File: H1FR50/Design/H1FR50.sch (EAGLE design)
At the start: 49 parts, among them J1 MOLEX_INC_0732511150MOLEX_INC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, P1 HEXABIT_17.32_X2_NO_P5, U1 STM32F091RBT6STMICROELECTRONI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, U2 TPS22943DCKR, U3 BGA824N6, U4 TESEO-LIV3F, U5 B39162B4327P810, X1 XTALL_CSTCE8M00G52

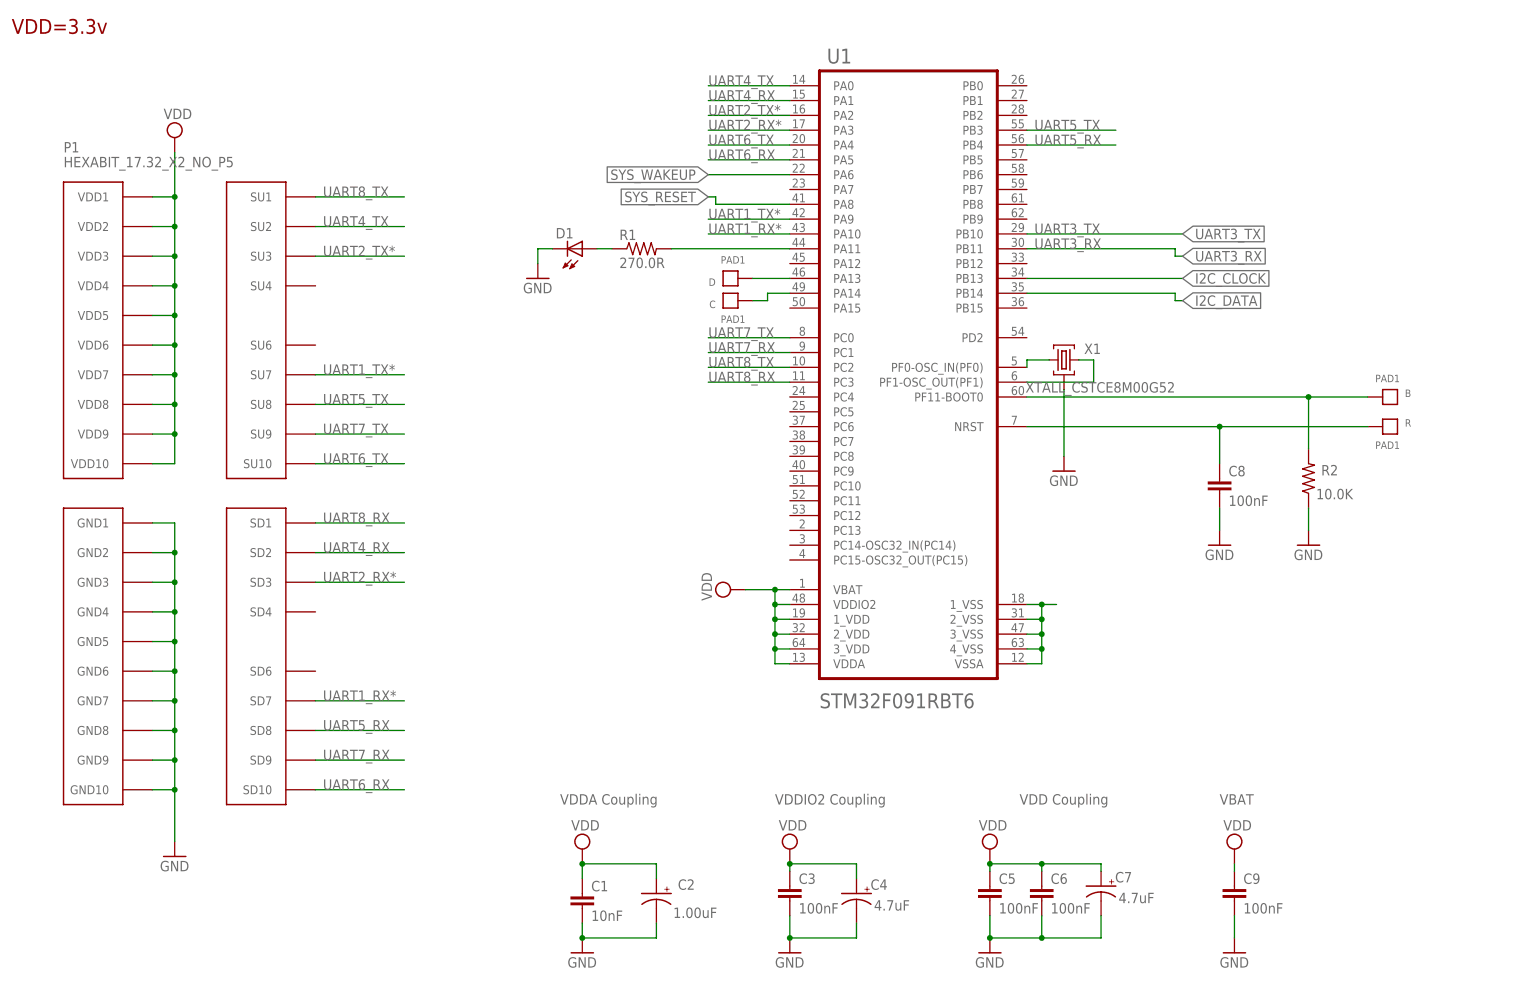
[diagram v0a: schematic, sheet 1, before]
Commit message: -Changing the MC to STM32G0B1CEU6N -Changing the GPS Module to SAM-M8Q-0-10 u-blox
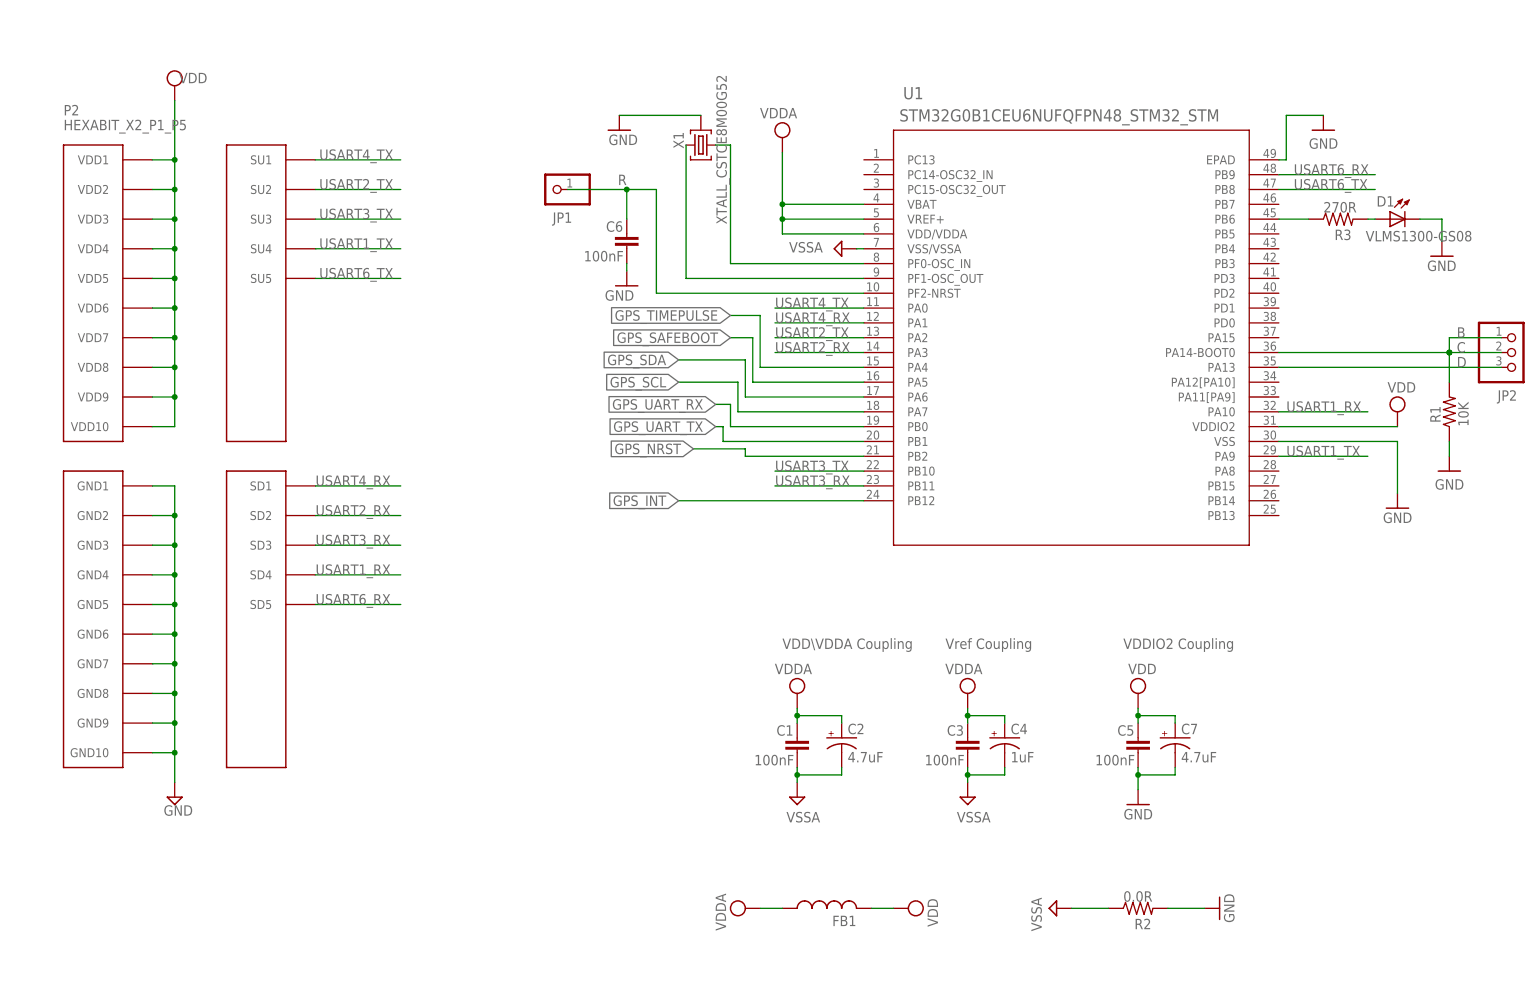
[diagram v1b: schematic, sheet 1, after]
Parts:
- removed B, C, D, R: PAD1, Hexabitz:PAD1
- removed C14: 3.9pF, HEXABITZ_RCLS:C-0402
- removed C15: 120pF, HEXABITZ_RCLS:C-0402
- removed C16: 1nF, HEXABITZ_RCLS:C-0402
- removed C17: 1.00uF, HEXABITZ_RCLS:C-0402
- removed C18: 2.2uF, HEXABITZ_RCLS:C-0402
- removed C19: 56pF, HEXABITZ_RCLS:C-0201C0201
- removed D2: ESDARF02-1BU2CK, HEXABITZ_RCLS:ESDARF02-1BU2CK
- removed FB4: 27nH, HEXABITZ_RCLS:FB-0402
- removed J1: MOLEX_INC_0732511150MOLEX_INC_0732511150_0_0, HEXABITZ_CONNECTION_PARTS:MOLEX_INC_0732511150MOLEX_INC_0732511150_0_0
- removed P1: HEXABIT_17.32_X2_NO_P5, hexabitz_connectors:HEXABIT_17.32_X2_NO_P5
- removed R10, R12: 0.0R, HEXABITZ_RCLS:R-0402
- removed R11, R13: DNP, HEXABITZ_RCLS:R-0402
- removed R14: 100k, HEXABITZ_RCLS:R-0603
- removed U3: BGA824N6, HEXABITZ_ICs:BGA824N6
- removed U4: TESEO-LIV3F, HEXABITZ_ICs:TESEO-LIV3F
- removed U5: B39162B4327P810, HEXABITZ_ICs:B39162B4327P810
- added FB1: (no value), HEXABITZ_RCLS:FB-0603
- added JP1: R, HEXABITZ_USER_INTERFACE_PARTS:PINHD-1X1
- added JP2: (no value), pinhead:PINHD-1X3
- added P2: HEXABIT_X2_P1_P5, hexabitz_connectors:HEXABIT_X2_P1_P5
- added Q1, Q2: MMBT3904LT1, HEXABITZ_RCLS:MMBT3904LT1
- added R3: 270R, HEXABITZ_RCLS:R-0603
- C1: value 10nF -> 100nF; device Hexabitz:C-0603 -> HEXABITZ_RCLS:C-0603; CAPACITANCE 10nF -> (none); MFN KEMET -> (none); MPN C0603C103K5RACTU -> (none); OCTOPART_URL https://octopart.com/c0603c103k5ractu-kemet-133094?r=sp&s=R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 -> (none); TOLERANCE 10% -> (none); VOLTAGE_RATING 50V -> (none)
- C10: value 56pF -> 100nF; device HEXABITZ_RCLS:C-0201C0201 -> HEXABITZ_RCLS:C-0603; MFN Murata -> (none); MPN GRM0335C1E560GA01D -> (none); OCTOPART_URL https://octopart.com/grm0335c1e560ga01d-murata-24611383?r=sp -> (none)
- C11: value 10nF -> 4.7uF; device HEXABITZ_RCLS:C-0402 -> HEXABITZ_RCLS:C-0805-POL; CAPACITANCE 10nF -> (none); MFN TDK -> (none); MPN CGA2B3X7R1H103K050BE -> (none); OCTOPART_URL https://octopart.com/cga2b3x7r1h103k050be-tdk-68305469?r=sp -> (none)
- C12: value 56pF -> 100nF; device HEXABITZ_RCLS:C-0402 -> HEXABITZ_RCLS:C-0603; CAPACITANCE 56pF -> (none); MFN Murata -> (none); MPN GRM1555C1H560JA01D -> (none); OCTOPART_URL https://octopart.com/grm1555c1h560ja01d-murata-15197568?r=sp -> (none)
- C13: value 120pF -> 4.7uF; device HEXABITZ_RCLS:C-0402 -> HEXABITZ_RCLS:C-0805-POL; CAPACITANCE 120pF -> (none); MFN Murata -> (none); MPN GRM1555C1H121JA01D -> (none); OCTOPART_URL https://octopart.com/grm1555c1h121ja01d-murata-196010?r=sp -> (none)
- C2: value 1.00uF -> 4.7uF; device Hexabitz:C-0805-POL -> HEXABITZ_RCLS:C-0805-POL; CAPACITANCE 1.00uF -> (none); MFN Yageo -> (none); MPN CC0805KKX7R7BB105 -> (none); OCTOPART_URL https://octopart.com/cc0805kkx7r7bb105-yageo-8376555?r=sp&s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 -> (none); TOLERANCE 10% -> (none); VOLTAGE_RATING 16V -> (none)
- C3, C6, C8: device Hexabitz:C-0603 -> HEXABITZ_RCLS:C-0603; CAPACITANCE 100nF -> (none); MFN KEMET -> (none); MPN C0603C104K8RACTU -> (none); OCTOPART_URL https://octopart.com/c0603c104k8ractu-kemet-145075?r=sp&s=9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 -> (none); TOLERANCE 10% -> (none); VOLTAGE_RATING 10V -> (none)
- C4: value 4.7uF -> 1uF; device Hexabitz:C-0805-POL -> HEXABITZ_RCLS:C-0805-POL; CAPACITANCE 4.7uF -> (none); MFN Murata -> (none); MPN GRM21BC81E475KA12L -> (none); OCTOPART_URL https://octopart.com/grm21bc81e475ka12l-murata-10331911?r=s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 -> (none); TOLERANCE 10% -> (none); VOLTAGE_RATING 25V -> (none)
- C5: device Hexabitz:C-0603 -> HEXABITZ_RCLS:C-0603; CAPACITANCE 100nF -> (none); MFN KEMET -> (none); MPN C0603C104K8RACTU -> (none); OCTOPART_URL https://octopart.com/c0603c104k8ractu-kemet-145075?r=sp&s=9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 -> (none); TOLERANCE 10% -> (none); VOLTAGE_RATING 10 -> (none)
- C7: device Hexabitz:C-0805-POL -> HEXABITZ_RCLS:C-0805-POL; CAPACITANCE 4.7uF -> (none); MFN Murata -> (none); MPN GRM21BC81E475KA12L -> (none); OCTOPART_URL https://octopart.com/grm21bc81e475ka12l-murata-10331911?r=s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 -> (none); TOLERANCE 10% -> (none); VOLTAGE_RATING 25V -> (none)
- C9: value 100nF -> 4.7uF; device Hexabitz:C-0603 -> HEXABITZ_RCLS:C-0805-POL; CAPACITANCE 100nF -> (none); MFN KEMET -> (none); MPN C0603C104K8RACTU -> (none); OCTOPART_URL https://octopart.com/c0603c104k8ractu-kemet-145075?r=sp&s=9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 -> (none); TOLERANCE 10V -> (none); VOLTAGE_RATING 10% -> (none)
- FB2: value 56nH -> BLM18KG601SN1D; device HEXABITZ_RCLS:FB-0402 -> HEXABITZ_RCLS:FB-0603; MFN Murata -> (none); MPN LQW15AN6N8G00D -> (none); OCTOPART_URL https://octopart.com/lqw15an6n8g00d-murata-7896134?r=sp -> (none)
- FB3: value 6.8nH -> BLM18KG601SN1D; device HEXABITZ_RCLS:FB-0402 -> HEXABITZ_RCLS:FB-0603; MFN Würth Elektronik -> (none); MPN 744784156A -> (none); OCTOPART_URL https://octopart.com/744784156a-w%C3%BCrth+elektronik-46756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 -> (none)
- R1: value 270.0R -> 10K; device Hexabitz:R-0603 -> HEXABITZ_RCLS:R-0603; MFN Yageo -> (none); MPN RC0603FR-07270RL -> (none); OCTOPART_URL https://octopart.com/search?q=RC0603FR-07270RL&start=0 -> (none); RESISTANCE 270.0 Ohm -> (none); TOLERANCE 1% -> (none)
- R2: value 10.0K -> 0.0R; device Hexabitz:R-0603 -> HEXABITZ_RCLS:R-0603; MFN Yageo -> (none); MPN RC0603JR-0710KL -> (none); OCTOPART_URL https://octopart.com/search?q=RC0603JR-0710KL&start=0 -> (none); RESISTANCE 10.0K Ohm -> (none); TOLERANCE 5% -> (none)
- R4: value 0.0R -> 10K; device HEXABITZ_RCLS:R-0402 -> HEXABITZ_RCLS:R-0603
- R5: value 10.0k -> 10K; device HEXABITZ_RCLS:R-0402 -> HEXABITZ_RCLS:R-0603; MFN TE Connectivity -> (none); MPN CRGCQ0402F10K -> (none); OCTOPART_URL https://octopart.com/crgcq0402f10k-te+connectivity-91017932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 -> (none); RESISTANCE 10.0K -> (none); TOLERANCE ±1% -> (none)
- R6, R7: value DNP -> 10K; device HEXABITZ_RCLS:R-0402 -> HEXABITZ_RCLS:R-0603
- R8: value 0.0R -> 150R; device HEXABITZ_RCLS:R-0402 -> HEXABITZ_RCLS:R-0603; MPN (none) -> CRCW0603150RFKEA
- R9: value DNP -> 150R; device HEXABITZ_RCLS:R-0402 -> HEXABITZ_RCLS:R-0603; MPN (none) -> CRCW0603150RFKEA
- U1: value STM32F091RBT6STMICROELECTRONICS_STM32F091RBT6_0_1 -> STM32G0B1CEU6NUFQFPN48_STM32_STM; device Hexabitz:STM32F091RBT6STMICROELECTRONICS_STM32F091RBT6_0_1 -> HEXABITZ_ICs:STM32G0B1CEU6NUFQFPN48_STM32_STM; MFN STMicroelectronics -> (none); OCTOPART_URL https://octopart.com/stm32f091rbt6-stmicroelectronics-51988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 -> (none)
- U2: value TPS22943DCKR -> SAM-M8Q-0-10; device HEXABITZ_ICs:TPS22943DCKR -> SAM-M8Q-0-10:SAM-M8Q-0-10
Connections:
- removed net ANTOFF: R10.2, R4.2, R5.1, U4.ANT_OFF
- removed net ANT_IN: R13.1, R6.1
- removed net B1: B.P$1, R2.2, U1.PF11-BOOT0
- removed net I2C_CLOCK: U1.PB13, U4.SCL
- removed net I2C_DATA: U1.PB14, U4.SDA
- removed net N$13: U3.AO, U5.INPUT
- removed net N$16: R4.1, R7.1, U3.PON
- removed net N$17: C15.1, U5.OUTPUT
- removed net N$19: C16.1, R8.1, U3.VCC
- removed net N$20: C17.1, R9.1, U2.VOUT
- removed net N$22: R10.1, R11.2, U2.ON
- removed net N$23: C18.1, R11.1, R12.2, R14.1, U2.VIN
- removed net R1: C8.1, R.P$1, U1.NRST
- removed net RF_IN: C15.2, R6.2, U4.RF_IN
- removed net SYS_RESET: U1.PA8, U4.SYS_RSTN
- removed net SYS_WAKEUP: U1.PA6, U4.WAKE-UP
- removed net UART1_RX*: P1.SD7, U1.PA10
- removed net UART1_TX*: P1.SU7, U1.PA9
- removed net UART2_RX*: P1.SD3, U1.PA3
- removed net UART2_TX*: P1.SU3, U1.PA2
- removed net UART3_RX: U1.PB11, U4.RX
- removed net UART3_TX: U1.PB10, U4.TX
- removed net UART4_RX: P1.SD2, U1.PA1
- removed net UART4_TX: P1.SU2, U1.PA0
- removed net UART5_RX: P1.SD8, U1.PB4
- removed net UART5_TX: P1.SU8, U1.PB3
- removed net UART6_RX: P1.SD10, U1.PA5
- removed net UART6_TX: P1.SU10, U1.PA4
- removed net UART7_RX: P1.SD9, U1.PC1
- removed net UART7_TX: P1.SU9, U1.PC0
- removed net UART8_RX: P1.SD1, U1.PC3
- removed net UART8_TX: P1.SU1, U1.PC2
- removed net VCC_RF: C19.2, R12.1, R7.2, R8.2, U4.VCC_RF
- removed net VCC_RF1: C10.2, FB4.1, U4.VBATT, U4.VCC, U4.VCC_IO
- new net C: JP2.1, JP2.2, R1.2, U1.PA14-BOOT0
- new net D: JP2.3, U1.PA13
- new net GPS_INT: U1.PB12, U2.EXTINT0
- new net GPS_NRST: R4.2, U1.PB2
- new net GPS_SAFEBOOT: R5.2, U1.PA5
- new net GPS_SCL: R8.2, U1.PA7
- new net GPS_SDA: R9.2, U1.PA6
- new net GPS_TIMEPULSE: U1.PA4, U2.TIMEPULSE
- new net GPS_UART_RX: FB2.2, U1.PB0
- new net GPS_UART_TX: FB3.2, U1.PB1
- new net N$14: R3.1, U1.PB6
- new net N$8: Q1.B, R5.1
- new net USART1_RX: P2.SD4, U1.PA10
- new net USART1_TX: P2.SU4, U1.PA9
- new net USART2_RX: P2.SD2, U1.PA3
- new net USART2_TX: P2.SU2, U1.PA2
- new net USART3_RX: P2.SD3, U1.PB11
- new net USART3_TX: P2.SU3, U1.PB10
- new net USART4_RX: P2.SD1, U1.PA1
- new net USART4_TX: P2.SU1, U1.PA0
- new net USART6_RX: P2.SD5, U1.PB9
- new net USART6_TX: P2.SU5, U1.PB8
- new net VDDA: C1.1, C2.+, C3.1, C4.+, FB1.1, U1.VBAT, U1.VDD/VDDA, U1.VREF+
- new net VSSA: C1.2, C2.-, C3.2, C4.-, R2.1, U1.VSS/VSSA
- net GND: now also C10.2, C11.-, C12.2, C13.-, C9.-, P2.GND1, P2.GND10, P2.GND2, P2.GND3, P2.GND4, P2.GND5, P2.GND6, P2.GND7, P2.GND8, P2.GND9, Q1.E, Q2.E, R1.1, R2.2, U1.EPAD, U1.VSS; no longer C1.2, C10.1, C11.1, C12.1, C14.1, C16.2, C17.2, C18.2, C19.1, C2.-, C3.2, C4.-, C9.2, D2.1, J1.MNT_1, J1.MNT_2, J1.MNT_3, J1.MNT_4, P1.GND1, P1.GND10, P1.GND2, P1.GND3, P1.GND4, P1.GND5, P1.GND6, P1.GND7, P1.GND8, P1.GND9, R2.1, R5.2, U1.1_VSS, U1.2_VSS, U1.3_VSS, U1.4_VSS, U1.VSSA, U3.GND, U3.GND-RF, U4.GND, U4.GND_RF_1, U4.GND_RF_2, U5.GND
- net N$1: now also D1.A, R3.2; no longer C13.2, C14.2, FB3.1
- net N$10: now also FB3.1, U2.TXD; no longer R1.2, U1.PA11
- net N$11: now also R8.1, U2.SCL; no longer C12.2, FB2.1, R9.2
- net N$12: now also R9.1, U2.SDA; no longer FB3.2, U3.AI
- net N$2: now also U1.PF0-OSC_IN, X1.3; no longer R14.2, U2.OC
- net N$3: now also U1.PF1-OSC_OUT, X1.1; no longer C13.1, D2.2, FB2.2, J1.1, R13.2
- net N$4: now also Q2.C, R7.1, U2.!RESET; no longer D1.A, R1.1
- net N$5: now also C6.1, JP1.1, U1.PF2-NRST; no longer U1.PF0-OSC_IN(PF0), X1.1
- net N$6: now also Q1.C, R6.1, U2.!SAFEBOOT; no longer U1.PF1-OSC_OUT(PF1), X1.3
- net N$7: now also Q2.B, R4.1; no longer D.P$1, U1.PA13
- net N$9: now also FB2.1, U2.RXD; no longer C.P$1, U1.PA14
- net VDD: now also C10.1, C11.+, C12.1, C13.+, C8.1, C9.+, FB1.2, P2.VDD1, P2.VDD10, P2.VDD2, P2.VDD3, P2.VDD4, P2.VDD5, P2.VDD6, P2.VDD7, P2.VDD8, P2.VDD9, R6.2, R7.2, U2.VCC, U2.VCC_IO, U2.V_BCKP; no longer C1.1, C11.2, C2.+, C3.1, C4.+, C6.1, C9.1, FB4.2, P1.VDD1, P1.VDD10, P1.VDD2, P1.VDD3, P1.VDD4, P1.VDD5, P1.VDD6, P1.VDD7, P1.VDD8, P1.VDD9, U1.1_VDD, U1.2_VDD, U1.3_VDD, U1.VBAT, U1.VDDA
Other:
- note added: "B"
- note added: "GPS Module"
- note added: "I2C2"
- note added: "Ibrahim Zaeiter"
- note added: "USART5"
- note added: "VDD=3.3 Volts"
- note added: "VDD\VDDA Coupling"
- note added: "Vref Coupling"
- note removed: "Anas Kaadan"
- note removed: "TESEO-LIV3F GNSS Module"
- note removed: "VBAT"
- note removed: "VDD Coupling"
- note removed: "VDD=3.3v"
- note removed: "VDDA Coupling"
- moved on the sheet: C1, C10, C12, C2, C3, C4, C5, C6, C7, D1, R1, R2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

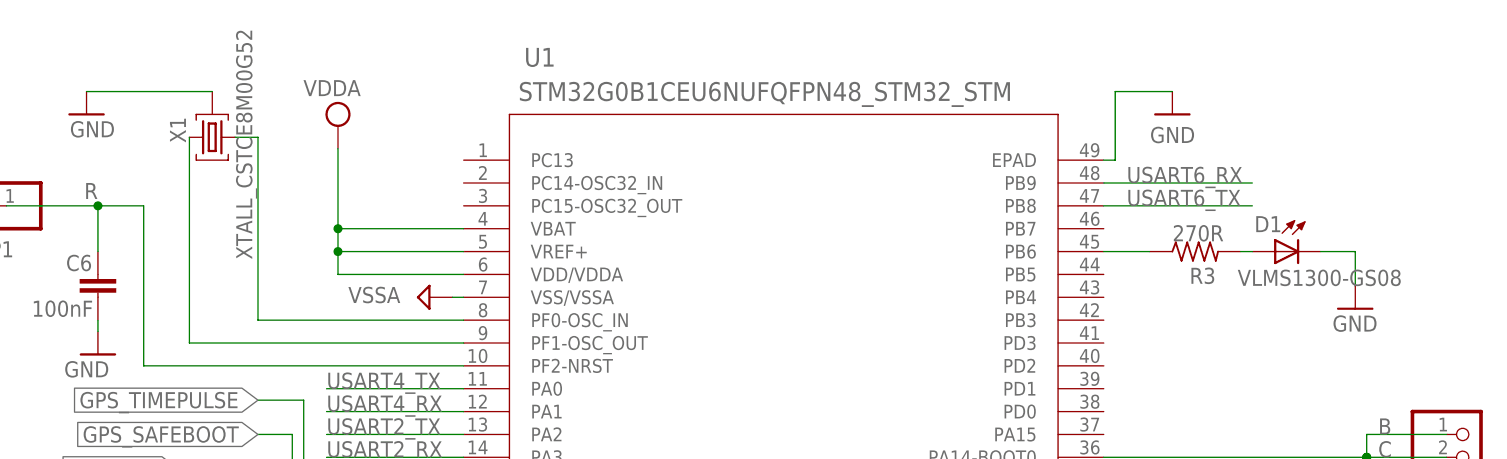
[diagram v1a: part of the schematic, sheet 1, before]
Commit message: -Correcting some documentaion issues
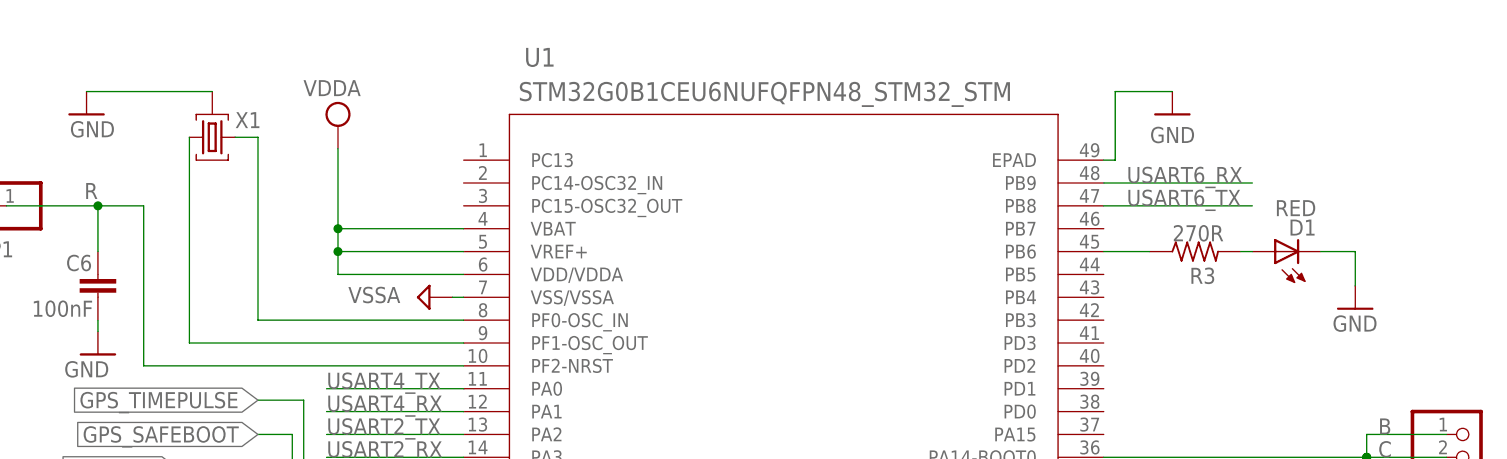
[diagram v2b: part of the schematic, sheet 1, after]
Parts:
- D1: value VLMS1300-GS08 -> RED; device Hexabitz:VLMS1300-GS08 -> HEXABITZ_USER_INTERFACE_PARTS:VLMS1300-GS08; MFN Vishay -> (none); MPN VLMS1300-GS08 -> (none); OCTOPART_URL https://octopart.com/vlms1300-gs08-vishay-21709201?r=sp&s=_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 -> (none)
- X1: value XTALL_CSTCE8M00G52 -> (none); device Hexabitz:XTALL_CSTCE8M00G52 -> HEXABITZ_RCLS:XTALL_CSTCE8M00G52
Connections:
- net N$2: now also X1.1; no longer X1.3
- net N$3: now also X1.3; no longer X1.1
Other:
- moved on the sheet: D1
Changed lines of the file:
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@@
 <?xml version="1.0" encoding="utf-8"?>
 <!DOCTYPE eagle SYSTEM "eagle.dtd">
-<eagle version="9.6.2">
+<eagle version="9.6.1">
 <drawing>
 <settings>
@@
 </classes>
 <parts>
-<part name="D1" library="Hexabitz" deviceset="VLMS1300-GS08" device="" value="VLMS1300-GS08">
-<attribute name="MFN" value="Vishay"/>
-<attribute name="MPN" value="VLMS1300-GS08"/>
-<attribute name="OCTOPART_URL" value="https://octopart.com/vlms1300-gs08-vishay-21709201?r=sp&amp;s=_gcP4_q8T1SC6PJQPTQ9yA"/>
-</part>
-<part name="X1" library="Hexabitz" deviceset="XTALL_CSTCE8M00G52" device="" value="XTALL_CSTCE8M00G52"/>
 <part name="GND1" library="supply1" library_urn="urn:adsk.eagle:library:371" deviceset="GND" device=""/>
 <part name="SUPPLY1" library="supply2" library_urn="urn:adsk.eagle:library:372" deviceset="VDD" device=""/>
 <part name="SUPPLY2" library="supply2" library_urn="urn:adsk.eagle:library:372" deviceset="GND" device=""/>
-<part name="P2" library="hexabitz_connectors" library_urn="urn:adsk.eagle:library:20064578" deviceset="HEXABIT_X2_P1_P5" device="" package3d_urn="urn:adsk.eagle:package:28065030/1"/>
+<part name="P2" library="hexabitz_connectors" library_urn="urn:adsk.eagle:library:20064578" deviceset="HEXABIT_X2_P1_P5" device="" package3d_urn="urn:adsk.eagle:package:28065030/1" override_package3d_urn="urn:adsk.eagle:package:28065030/2" override_package_urn="urn:adsk.eagle:footprint:28065029/1"/>
 <part name="SUPPLY14" library="supply2" deviceset="VDD" device=""/>
 <part name="SUPPLY15" library="supply2" deviceset="VCC" device="" value="VDDA"/>
@@
 <part name="SUPPLY9" library="supply2" deviceset="VDD" device=""/>
 <part name="JP2" library="pinhead" deviceset="PINHD-1X3" device="" package3d_urn="urn:adsk.eagle:package:22458/2"/>
-<part name="U2" library="SAM-M8Q-0-10" deviceset="SAM-M8Q-0-10" device=""/>
+<part name="U2" library="SAM-M8Q-0-10" deviceset="SAM-M8Q-0-10" device="" override_package3d_urn="urn:adsk.eagle:package:37789442/2" override_package_urn="urn:adsk.eagle:footprint:37789443/1"/>
 <part name="SUPPLY5" library="supply2" deviceset="VDD" device=""/>
 <part name="GND4" library="supply1" library_urn="urn:adsk.eagle:library:371" deviceset="GND" device=""/>
@@
 <attribute name="MPN" value="CRCW0603150RFKEA"/>
 </part>
-<part name="U1" library="HEXABITZ_ICs" library_urn="urn:adsk.eagle:library:20064554" deviceset="STM32G0B1CEU6N" device="UFQFPN48_STM32_STM" package3d_urn="urn:adsk.eagle:package:33906703/3"/>
+<part name="U1" library="HEXABITZ_ICs" library_urn="urn:adsk.eagle:library:20064554" deviceset="STM32G0B1CEU6N" device="UFQFPN48_STM32_STM" package3d_urn="urn:adsk.eagle:package:33906703/4"/>
+<part name="D1" library="HEXABITZ_USER_INTERFACE_PARTS" library_urn="urn:adsk.eagle:library:20064563" deviceset="VLMS1300-GS08" device="" package3d_urn="urn:adsk.eagle:package:20064571/2" value="RED"/>
+<part name="X1" library="HEXABITZ_RCLS" library_urn="urn:adsk.eagle:library:20064561" deviceset="XTALL_CSTCE8M00G52" device="" package3d_urn="urn:adsk.eagle:package:20410717/1" override_package3d_urn="urn:adsk.eagle:package:20410717/2" override_package_urn="urn:adsk.eagle:footprint:20410716/1"/>
 </parts>
 <sheets>
@@
 </plain>
 <instances>
-<instance part="D1" gate="G$1" x="251.46" y="168.91" smashed="yes" rot="MR0">
-<attribute name="NAME" x="252.222" y="171.069" size="1.778" layer="95" rot="MR0"/>
-<attribute name="VALUE" x="265.557" y="165.1" size="1.778" layer="96" rot="MR0"/>
-</instance>
-<instance part="X1" gate="G$1" x="133.35" y="181.61" smashed="yes" rot="MR180">
-<attribute name="NAME" x="128.651" y="180.975" size="1.778" layer="95" rot="MR90"/>
-<attribute name="VALUE" x="137.795" y="193.675" size="1.778" layer="96" rot="MR270"/>
-</instance>
 <instance part="GND1" gate="1" x="260.35" y="162.56" smashed="yes">
 <attribute name="VALUE" x="257.81" y="160.02" size="1.778" layer="96"/>
@@
 <attribute name="VALUE" x="167.3552" y="185.6486" size="2.083" layer="96" ratio="6"/>
 </instance>
+<instance part="D1" gate="G$1" x="251.46" y="168.91" smashed="yes" rot="R180">
+<attribute name="NAME" x="256.032" y="172.466" size="1.778" layer="95" rot="R180"/>
+<attribute name="VALUE" x="256.032" y="174.625" size="1.778" layer="96" rot="R180"/>
+</instance>
+<instance part="X1" gate="G$1" x="133.35" y="181.61" smashed="yes" rot="R180">
+<attribute name="NAME" x="135.89" y="182.626" size="1.778" layer="95"/>
+<attribute name="VALUE" x="135.89" y="179.07" size="1.778" layer="96"/>
+</instance>
 </instances>
 <busses>
@@
 </segment>
 <segment>
-<pinref part="X1" gate="G$1" pin="2"/>
 <pinref part="GND10" gate="1" pin="GND"/>
 <wire x1="133.35" y1="186.69" x2="119.38" y2="186.69" width="0.1524" layer="91"/>
+<pinref part="X1" gate="G$1" pin="2"/>
 </segment>
 <segment>
@@
 </segment>
 <segment>
-<pinref part="D1" gate="G$1" pin="C"/>
 <pinref part="GND1" gate="1" pin="GND"/>
 <wire x1="256.54" y1="168.91" x2="260.35" y2="168.91" width="0.1524" layer="91"/>
 <wire x1="260.35" y1="168.91" x2="260.35" y2="165.1" width="0.1524" layer="91"/>
+<pinref part="D1" gate="G$1" pin="C"/>
 </segment>
 <segment>
@@
 <net name="N$1" class="0">
 <segment>
-<pinref part="D1" gate="G$1" pin="A"/>
 <wire x1="248.92" y1="168.91" x2="247.65" y2="168.91" width="0.1524" layer="91"/>
 <pinref part="R3" gate="G$1" pin="2"/>
+<pinref part="D1" gate="G$1" pin="A"/>
 </segment>
 </net>
@@
 <net name="N$2" class="0">
 <segment>
-<pinref part="X1" gate="G$1" pin="3"/>
 <wire x1="135.89" y1="181.61" x2="138.43" y2="181.61" width="0.1524" layer="91"/>
 <wire x1="138.43" y1="181.61" x2="138.43" y2="161.29" width="0.1524" layer="91"/>
 <wire x1="138.43" y1="161.29" x2="161.29" y2="161.29" width="0.1524" layer="91"/>
 <pinref part="U1" gate="A" pin="PF0-OSC_IN"/>
+<pinref part="X1" gate="G$1" pin="1"/>
 </segment>
 </net>
 <net name="N$3" class="0">
 <segment>
-<pinref part="X1" gate="G$1" pin="1"/>
 <wire x1="161.29" y1="158.75" x2="130.81" y2="158.75" width="0.1524" layer="91"/>
 <wire x1="130.81" y1="158.75" x2="130.81" y2="181.61" width="0.1524" layer="91"/>
 <pinref part="U1" gate="A" pin="PF1-OSC_OUT"/>
+<pinref part="X1" gate="G$1" pin="3"/>
 </segment>
 </net>
@@
 packages will not be understood (or retained) with this version.
 </note>
+<note version="9.4" severity="warning">
+Since Version 9.4, EAGLE supports the overriding of 3D packages
+in schematics and board files. Those overridden 3d packages
+will not be understood (or retained) with this version.
+</note>
 </compatibility>
